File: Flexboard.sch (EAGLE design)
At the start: 438 parts, among them J1 USB4105-GF-A, SW1 1825910-7, U1 MK22FX512AVLQ12, Y1 ABM3B-8.000MHZ-B2-T, Y2 ABS07-32.768KHZ-T

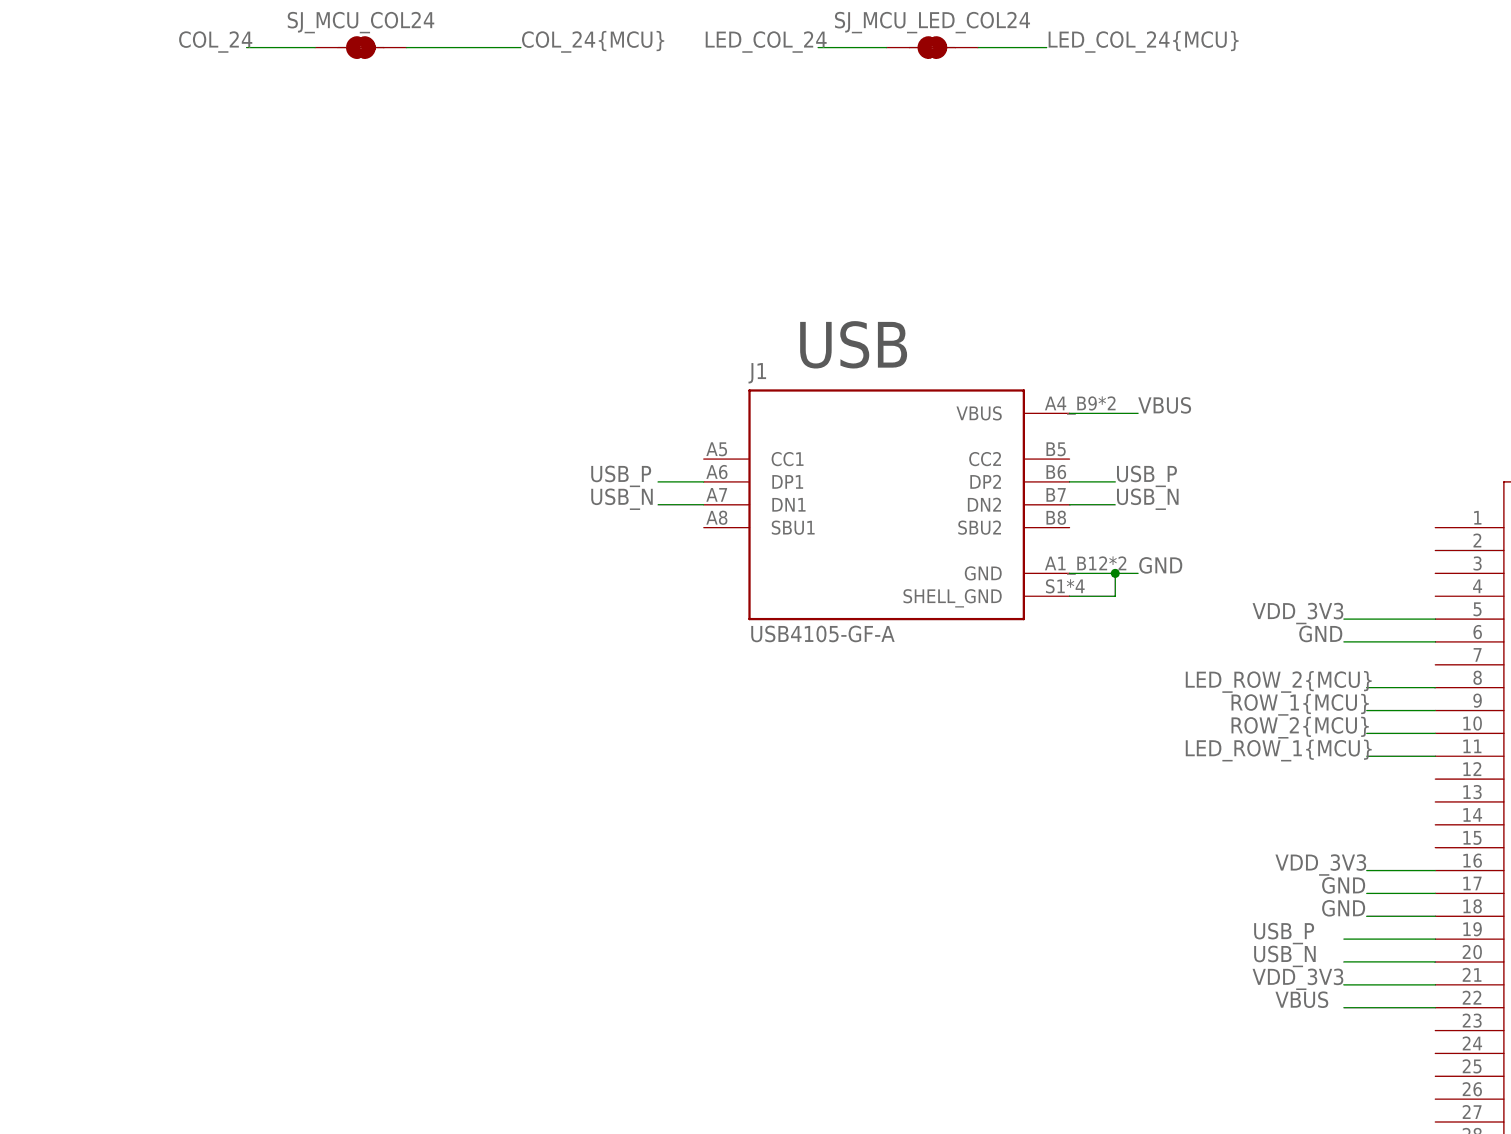
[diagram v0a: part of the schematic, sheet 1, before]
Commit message: added usb 33 ohm resistors
Added 33 ohm resistors to usb traces, and redid length matching

Signed-off-by: Daniel DeGrasse <daniel@degrasse.com>
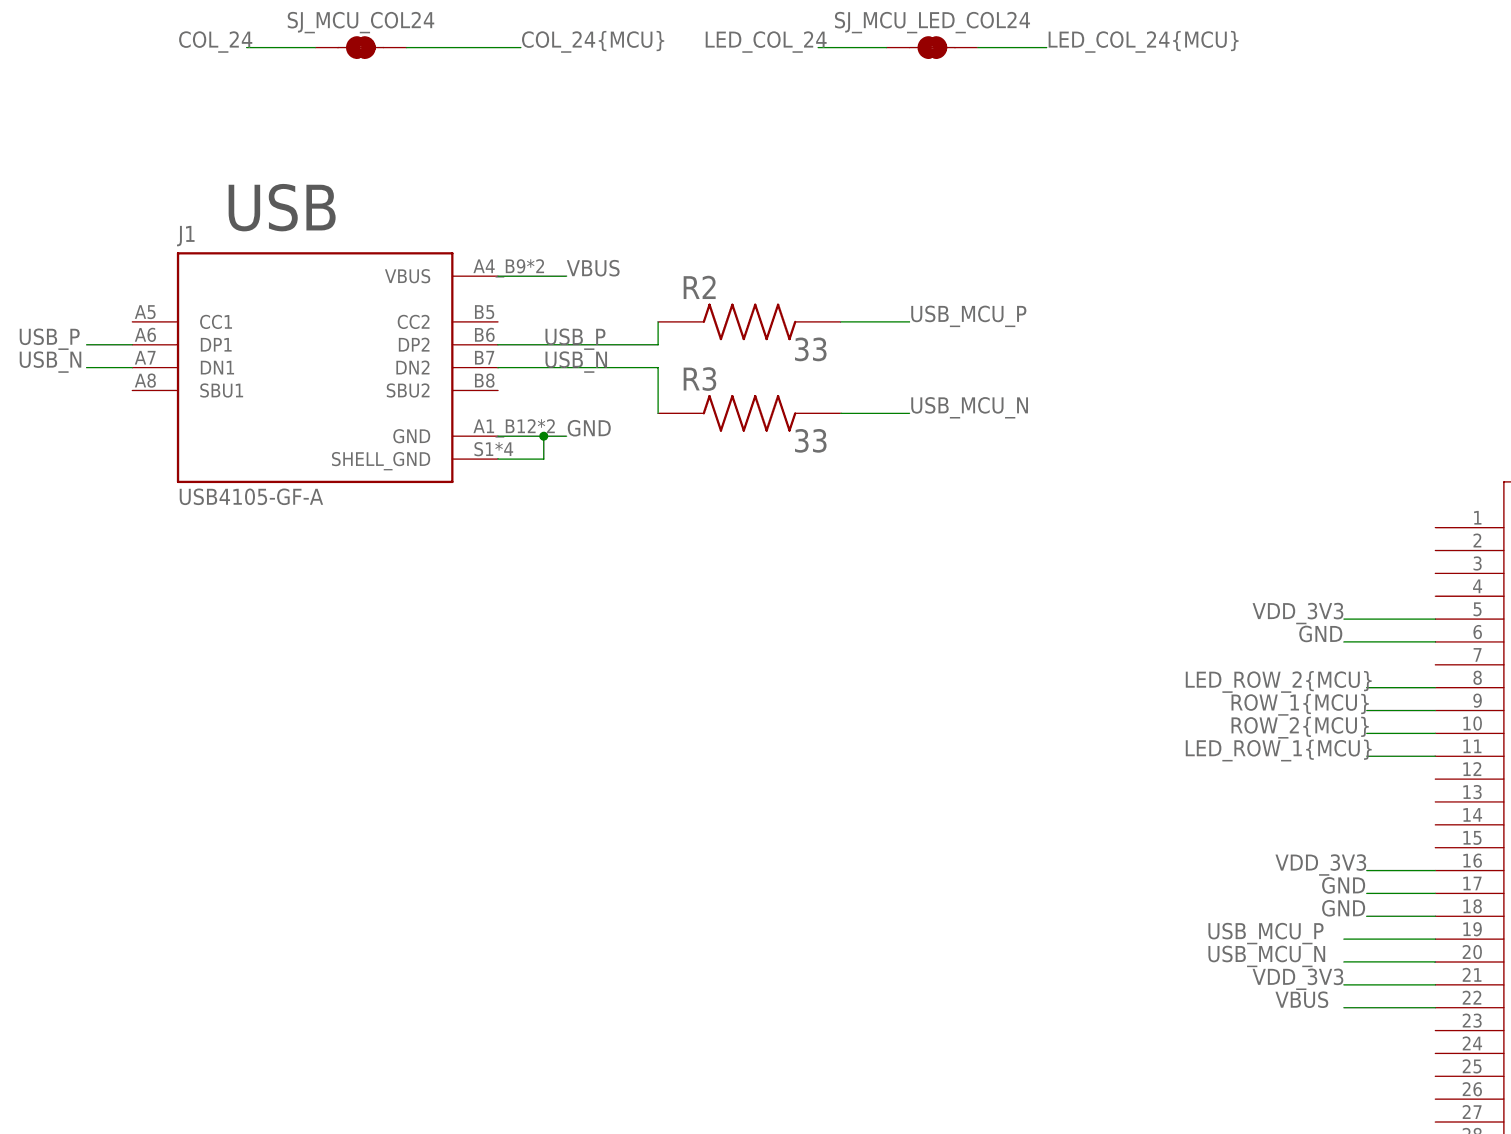
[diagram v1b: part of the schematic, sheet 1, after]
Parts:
- added R2, R3: 33, CRG0805F33R:CRG0805F33R
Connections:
- new net USB_MCU_N: R3.2, U1A.USB0_DM
- new net USB_MCU_P: R2.2, U1A.USB0_DP
- net USB_N: now also R3.1; no longer U1A.USB0_DM
- net USB_P: now also R2.1; no longer U1A.USB0_DP
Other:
- moved on the sheet: J1
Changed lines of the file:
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@@
 <part name="C11" library="C1206C220JGGAC7800" deviceset="C1206C220JGGAC7800" device="" value="22pF"/>
 <part name="Y2" library="ABS07-32.768KHZ-T" deviceset="ABS07-32.768KHZ-T" device=""/>
+<part name="R2" library="CRG0805F33R" deviceset="CRG0805F33R" device="" value="33"/>
+<part name="R3" library="CRG0805F33R" deviceset="CRG0805F33R" device="" value="33"/>
 </parts>
 <sheets>
@@
 <description>Microcontroller Schematic</description>
 <plain>
-<text x="-119.38" y="86.36" size="5.08" layer="97">USB</text>
+<text x="-182.88" y="101.6" size="5.08" layer="97">USB</text>
 <text x="-154.94" y="307.34" size="5.08" layer="97">Solder Bridges</text>
 <text x="25.4" y="83.82" size="5.08" layer="97">MCU</text>
@@
 <attribute name="NAME" x="-104.14" y="124.968" size="1.778" layer="95" font="vector" align="center"/>
 </instance>
-<instance part="J1" gate="G$1" x="-109.22" y="71.12" smashed="yes">
-<attribute name="NAME" x="-124.46" y="85.09" size="1.778" layer="95"/>
-<attribute name="VALUE" x="-124.46" y="55.88" size="1.778" layer="96"/>
+<instance part="J1" gate="G$1" x="-172.72" y="86.36" smashed="yes">
+<attribute name="NAME" x="-187.96" y="100.33" size="1.778" layer="95"/>
+<attribute name="VALUE" x="-187.96" y="71.12" size="1.778" layer="96"/>
 </instance>
 <instance part="U$1" gate="G$1" x="264.16" y="71.12" smashed="yes">
@@
 <attribute name="NAME" x="259.325690625" y="17.78436875" size="1.781059375" layer="95"/>
 <attribute name="VALUE" x="259.323540625" y="11.167190625" size="1.78185" layer="96"/>
+</instance>
+<instance part="R2" gate="G$1" x="-124.46" y="91.44" smashed="yes">
+<attribute name="NAME" x="-132.084440625" y="93.98148125" size="2.54148125" layer="95"/>
+<attribute name="VALUE" x="-119.64396875" y="87.115359375" size="2.54331875" layer="96"/>
+</instance>
+<instance part="R3" gate="G$1" x="-124.46" y="81.28" smashed="yes">
+<attribute name="NAME" x="-132.084440625" y="83.82148125" size="2.54148125" layer="95"/>
+<attribute name="VALUE" x="-119.64396875" y="76.955359375" size="2.54331875" layer="96"/>
 </instance>
 </instances>
@@
 <segment>
 <pinref part="J1" gate="G$1" pin="GND"/>
-<wire x1="-88.9" y1="63.5" x2="-83.82" y2="63.5" width="0.1524" layer="91"/>
+<wire x1="-152.4" y1="78.74" x2="-147.32" y2="78.74" width="0.1524" layer="91"/>
 <pinref part="J1" gate="G$1" pin="SHELL_GND"/>
-<wire x1="-83.82" y1="63.5" x2="-81.28" y2="63.5" width="0.1524" layer="91"/>
-<wire x1="-88.9" y1="60.96" x2="-83.82" y2="60.96" width="0.1524" layer="91"/>
-<wire x1="-83.82" y1="60.96" x2="-83.82" y2="63.5" width="0.1524" layer="91"/>
-<junction x="-83.82" y="63.5"/>
-<label x="-81.28" y="63.5" size="1.778" layer="95"/>
+<wire x1="-147.32" y1="78.74" x2="-144.78" y2="78.74" width="0.1524" layer="91"/>
+<wire x1="-152.4" y1="76.2" x2="-147.32" y2="76.2" width="0.1524" layer="91"/>
+<wire x1="-147.32" y1="76.2" x2="-147.32" y2="78.74" width="0.1524" layer="91"/>
+<junction x="-147.32" y="78.74"/>
+<label x="-144.78" y="78.74" size="1.778" layer="95"/>
 </segment>
 <segment>
@@
 <net name="USB_P" class="0">
 <segment>
-<pinref part="U1" gate="A" pin="USB0_DP"/>
-<wire x1="-48.26" y1="22.86" x2="-58.42" y2="22.86" width="0.1524" layer="91"/>
-<label x="-68.58" y="22.86" size="1.778" layer="95"/>
-</segment>
-<segment>
 <pinref part="J1" gate="G$1" pin="DP2"/>
-<wire x1="-88.9" y1="73.66" x2="-83.82" y2="73.66" width="0.1524" layer="91"/>
-<label x="-83.82" y="73.66" size="1.778" layer="95"/>
+<label x="-147.32" y="88.9" size="1.778" layer="95"/>
+<wire x1="-152.4" y1="88.9" x2="-134.62" y2="88.9" width="0.1524" layer="91"/>
+<wire x1="-134.62" y1="88.9" x2="-134.62" y2="91.44" width="0.1524" layer="91"/>
+<pinref part="R2" gate="G$1" pin="1"/>
 </segment>
 <segment>
 <pinref part="J1" gate="G$1" pin="DP1"/>
-<wire x1="-129.54" y1="73.66" x2="-134.62" y2="73.66" width="0.1524" layer="91"/>
-<label x="-142.24" y="73.66" size="1.778" layer="95"/>
+<wire x1="-193.04" y1="88.9" x2="-198.12" y2="88.9" width="0.1524" layer="91"/>
+<label x="-205.74" y="88.9" size="1.778" layer="95"/>
 </segment>
 </net>
 <net name="USB_N" class="0">
 <segment>
-<pinref part="U1" gate="A" pin="USB0_DM"/>
-<wire x1="-48.26" y1="20.32" x2="-58.42" y2="20.32" width="0.1524" layer="91"/>
-<label x="-68.58" y="20.32" size="1.778" layer="95"/>
-</segment>
-<segment>
 <pinref part="J1" gate="G$1" pin="DN2"/>
-<wire x1="-88.9" y1="71.12" x2="-83.82" y2="71.12" width="0.1524" layer="91"/>
-<label x="-83.82" y="71.12" size="1.778" layer="95"/>
+<label x="-147.32" y="86.36" size="1.778" layer="95"/>
+<wire x1="-134.62" y1="81.28" x2="-134.62" y2="86.36" width="0.1524" layer="91"/>
+<wire x1="-134.62" y1="86.36" x2="-152.4" y2="86.36" width="0.1524" layer="91"/>
+<pinref part="R3" gate="G$1" pin="1"/>
 </segment>
 <segment>
 <pinref part="J1" gate="G$1" pin="DN1"/>
-<wire x1="-129.54" y1="71.12" x2="-134.62" y2="71.12" width="0.1524" layer="91"/>
-<label x="-142.24" y="71.12" size="1.778" layer="95"/>
+<wire x1="-193.04" y1="86.36" x2="-198.12" y2="86.36" width="0.1524" layer="91"/>
+<label x="-205.74" y="86.36" size="1.778" layer="95"/>
 </segment>
 </net>
@@
 <segment>
 <pinref part="J1" gate="G$1" pin="VBUS"/>
-<wire x1="-88.9" y1="81.28" x2="-81.28" y2="81.28" width="0.1524" layer="91"/>
-<label x="-81.28" y="81.28" size="1.778" layer="95"/>
+<wire x1="-152.4" y1="96.52" x2="-144.78" y2="96.52" width="0.1524" layer="91"/>
+<label x="-144.78" y="96.52" size="1.778" layer="95"/>
 </segment>
 </net>
@@
 </segment>
 </net>
+<net name="USB_MCU_P" class="0">
+<segment>
+<pinref part="U1" gate="A" pin="USB0_DP"/>
+<wire x1="-48.26" y1="22.86" x2="-58.42" y2="22.86" width="0.1524" layer="91"/>
+<label x="-73.66" y="22.86" size="1.778" layer="95"/>
+</segment>
+<segment>
+<wire x1="-114.3" y1="91.44" x2="-106.68" y2="91.44" width="0.1524" layer="91"/>
+<label x="-106.68" y="91.44" size="1.778" layer="95"/>
+<pinref part="R2" gate="G$1" pin="2"/>
+</segment>
+</net>
+<net name="USB_MCU_N" class="0">
+<segment>
+<pinref part="U1" gate="A" pin="USB0_DM"/>
+<wire x1="-48.26" y1="20.32" x2="-58.42" y2="20.32" width="0.1524" layer="91"/>
+<label x="-73.66" y="20.32" size="1.778" layer="95"/>
+</segment>
+<segment>
+<wire x1="-114.3" y1="81.28" x2="-106.68" y2="81.28" width="0.1524" layer="91"/>
+<label x="-106.68" y="81.28" size="1.778" layer="95"/>
+<pinref part="R3" gate="G$1" pin="2"/>
+</segment>
+</net>

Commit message: added TVS diodes for ESD protection and power source switch
TVS diodes required for high voltage spike protection, power
source switch will enable selection of LDO or internal regulator

Signed-off-by: Daniel DeGrasse <daniel@degrasse.com>
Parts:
- added C12: 2.2uF, 1206ZC225MAT2A:1206ZC225MAT2A
- added C13: 10uF, GRM21BC8YA106ME11L:GRM21BC8YA106ME11L
- added L1, L2: 330, 782853331:782853331SMD
- added SJ1: (no value), jumper:SJ2W
- added SV1: (no value), con-lstb:MA04-1
- added TVS1, TVS2, TVS3: (no value), 0603ESDA2-TR2:0603ESDA2-TR2
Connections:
- new net N$1: J1.SHELL_GND, L2.1
- new net UART0_RX: SV1.3, U1B.PTB16
- new net UART0_TX: SV1.2, U1B.PTB17
- new net VLDO_33: SJ1.1
- new net VOUT_33: C12.1, SJ1.3, U1A.VOUT33
- new net VSYS_5V5: C13.1, L1.2, U1A.VREGIN
- net GND: now also C12.2, C13.2, L2.2, SV1.4, TVS1.2, TVS2.1, TVS3.1; no longer J1.SHELL_GND
- net USB_N: now also TVS2.2
- net USB_P: now also TVS3.2
- net VBUS: now also L1.1, TVS1.1; no longer U1A.VREGIN
- net VDD_3V3: now also SJ1.2, SV1.1; no longer U1A.VOUT33
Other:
- note added: "Power Decoupling"
- note added: "Power Source Selection"
- note added: "UART"
- moved on the sheet: J1, R2, R3

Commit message: added LDO to design
LDO added, now just need power decoupling caps and diodes
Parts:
- added U2: NCP1117ST33T3G, NCP1117ST33T3G:NCP1117ST33T3G
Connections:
- net GND: now also U2.GND
- net VLDO_33: now also U2.OUT
- net VSYS_5V5: now also U2.IN
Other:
- note added: "LDO"
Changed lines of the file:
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@@
 <part name="TVS3" library="0603ESDA2-TR2" deviceset="0603ESDA2-TR2" device=""/>
 <part name="C13" library="GRM21BC8YA106ME11L" deviceset="GRM21BC8YA106ME11L" device="" value="10uF"/>
+<part name="U2" library="NCP1117ST33T3G" deviceset="NCP1117ST33T3G" device=""/>
 </parts>
 <sheets>
@@
 <text x="-223.52" y="53.34" size="5.08" layer="97">Power Source Selection</text>
 <text x="17.78" y="137.16" size="5.08" layer="97">Power Decoupling</text>
+<text x="-228.6" y="20.32" size="5.08" layer="97">LDO</text>
 </plain>
 <instances>
@@
 <attribute name="NAME" x="151.13093125" y="119.38" size="1.77843125" layer="95" rot="R270"/>
 <attribute name="VALUE" x="142.23151875" y="119.38" size="1.78096875" layer="96" rot="R270"/>
+</instance>
+<instance part="U2" gate="G$1" x="-223.52" y="10.16" smashed="yes">
+<attribute name="NAME" x="-233.6826" y="17.78196875" size="1.778459375" layer="95"/>
+<attribute name="VALUE" x="-236.2315" y="2.53308125" size="1.779609375" layer="96"/>
 </instance>
 </instances>
@@
 <label x="147.32" y="109.22" size="1.778" layer="95"/>
 </segment>
+<segment>
+<pinref part="U2" gate="G$1" pin="GND"/>
+<wire x1="-205.74" y1="7.62" x2="-193.04" y2="7.62" width="0.1524" layer="91"/>
+<label x="-193.04" y="7.62" size="1.778" layer="95"/>
+</segment>
 </net>
 <net name="ROW_5{SB}" class="0">
@@
 <label x="-203.2" y="38.1" size="1.778" layer="95"/>
 </segment>
+<segment>
+<pinref part="U2" gate="G$1" pin="OUT"/>
+<wire x1="-205.74" y1="12.7" x2="-193.04" y2="12.7" width="0.1524" layer="91"/>
+<label x="-193.04" y="12.7" size="1.778" layer="95"/>
+</segment>
 </net>
 <net name="VSYS_5V5" class="0">
@@
 <label x="147.32" y="127" size="1.778" layer="95"/>
 </segment>
-</net>
+<segment>
+<pinref part="U2" gate="G$1" pin="IN"/>
+<wire x1="-241.3" y1="10.16" x2="-256.54" y2="10.16" width="0.1524" layer="91"/>
+<label x="-256.54" y="10.16" size="1.778" layer="95"/>
+</segment>
+</net>

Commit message: added all power domain components
Added schottky diode on 5V LDO power rail to protect LDO. Power domain
routing should be complete.
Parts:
- added C14: 10uF, GRM21BC8YA106ME11L:GRM21BC8YA106ME11L
- added D146: UPS115UE3/TR7, UPS115UE3-TR7:UPS115UE3/TR7
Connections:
- new net VLDO_5V5: D146.P$1, U2.IN
- net GND: now also C14.2
- net VLDO_33: now also C14.1
- net VSYS_5V5: now also D146.P$2; no longer U2.IN
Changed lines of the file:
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@@
 <part name="C13" library="GRM21BC8YA106ME11L" deviceset="GRM21BC8YA106ME11L" device="" value="10uF"/>
 <part name="U2" library="NCP1117ST33T3G" deviceset="NCP1117ST33T3G" device=""/>
+<part name="D146" library="UPS115UE3-TR7" deviceset="UPS115UE3/TR7" device=""/>
+<part name="C14" library="GRM21BC8YA106ME11L" deviceset="GRM21BC8YA106ME11L" device="" value="10uF"/>
 </parts>
 <sheets>
@@
 <attribute name="NAME" x="-233.6826" y="17.78196875" size="1.778459375" layer="95"/>
 <attribute name="VALUE" x="-236.2315" y="2.53308125" size="1.779609375" layer="96"/>
+</instance>
+<instance part="D146" gate="G$1" x="-256.54" y="10.16" smashed="yes" rot="R180">
+<attribute name="NAME" x="-251.46" y="5.08" size="2.54" layer="95" rot="R180"/>
+<attribute name="VALUE" x="-251.46" y="17.78" size="2.54" layer="96" rot="R180"/>
+</instance>
+<instance part="C14" gate="G$1" x="167.64" y="119.38" smashed="yes" rot="R270">
+<attribute name="NAME" x="171.45093125" y="119.38" size="1.77843125" layer="95" rot="R270"/>
+<attribute name="VALUE" x="162.55151875" y="119.38" size="1.78096875" layer="96" rot="R270"/>
 </instance>
 </instances>
@@
 <label x="-193.04" y="7.62" size="1.778" layer="95"/>
 </segment>
+<segment>
+<pinref part="C14" gate="G$1" pin="2"/>
+<label x="167.64" y="109.22" size="1.778" layer="95"/>
+<wire x1="167.64" y1="114.3" x2="167.64" y2="109.22" width="0.1524" layer="91"/>
+</segment>
 </net>
 <net name="ROW_5{SB}" class="0">
@@
 <label x="-193.04" y="12.7" size="1.778" layer="95"/>
 </segment>
+<segment>
+<pinref part="C14" gate="G$1" pin="1"/>
+<wire x1="167.64" y1="121.92" x2="167.64" y2="127" width="0.1524" layer="91"/>
+<label x="167.64" y="127" size="1.778" layer="95"/>
+</segment>
 </net>
 <net name="VSYS_5V5" class="0">
@@
 </segment>
 <segment>
-<pinref part="U2" gate="G$1" pin="IN"/>
-<wire x1="-241.3" y1="10.16" x2="-256.54" y2="10.16" width="0.1524" layer="91"/>
-<label x="-256.54" y="10.16" size="1.778" layer="95"/>
+<wire x1="-264.16" y1="10.16" x2="-276.86" y2="10.16" width="0.1524" layer="91"/>
+<label x="-276.86" y="10.16" size="1.778" layer="95"/>
+<pinref part="D146" gate="G$1" pin="P$2"/>
 </segment>
 </net>
@@
 </segment>
 </net>
+<net name="VLDO_5V5" class="0">
+<segment>
+<pinref part="U2" gate="G$1" pin="IN"/>
+<wire x1="-251.46" y1="10.16" x2="-241.3" y2="10.16" width="0.1524" layer="91"/>
+<pinref part="D146" gate="G$1" pin="P$1"/>
+<label x="-250.698" y="7.874" size="1.778" layer="95"/>
+</segment>
+</net>
